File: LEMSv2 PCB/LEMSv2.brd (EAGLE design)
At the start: 160 x 100 mm, 83 parts, among them J2 M05, Q1 200mA/50V, Q10 200mA/50V, Q2 200mA/50V, Q3 200mA/50V, Q4 200mA/50V, Q5 200mA/50V, Q6 200mA/50V, Q7 200mA/50V, Q8 MMBT3904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

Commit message: Modified SD connector footprint, moved connectors
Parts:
- U1: value SDMMC06132 -> (none)
- moved J3 109.0 mm to (57.1, 17.1)
- moved J4 108.6 mm to (36.8, 17.1)
- moved J1 83.2 mm to (64.9, 42.5), turned to 270 degrees
- moved J5 78.9 mm to (54.6, 65.4)
- moved J6 73.4 mm to (30.2, 65.4)
- moved J2 61.7 mm to (40.6, 24.8)
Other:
- board outline removed

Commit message: Initial layout
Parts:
- removed D1: GREEN, LEMSv2:LED-0603
- removed D2: RED, LEMSv2:LED-0603
- added LED1: GREEN, LEMSv2:LED-0603
- added LED2: RED, LEMSv2:LED-0603
- C2, C3, C4, C5, C6, C7, C8, FB1: device LEMSv2:0805 -> LEMSv2:_0805
- J1: value (none) -> FEMALE 2x3; device LEMSv2:2X3_SMD -> LEMSv2:2X3
- J2: value M05 -> (none); device LEMSv2:1X05_SMD -> SparkFun-Connectors:1X05
- J3: device LEMSv2:1X06_SMD_STRAIGHT_COMBO -> LEMSv2:1X06
- J4, J5: device LEMSv2:1X08_SMD_COMBINED -> LEMSv2:1X08_ROUND
- J6: device LEMSv2:1X10_SMD_COMBINED -> LEMSv2:1X10
- moved U$3 173.9 mm to (81.3, 34.3), turned to 90 degrees
- moved U$1 156.4 mm to (81.3, 67.9)
- moved J26 152.6 mm to (80.6, 60.3), turned to 90 degrees
- moved C1 146.5 mm to (61.6, 35.6), turned to 270 degrees
- moved J17 139.8 mm to (73.8, 67.9), turned to 180 degrees
- moved Q9 138.4 mm to (64.8, 41.9)
- moved Q8 133.3 mm to (64.8, 46.4)
- moved R11 132.9 mm to (36.8, 24.1), turned to 180 degrees
- moved S1 132.4 mm to (81.3, 43.8), turned to 180 degrees
- moved J19 129.6 mm to (45.8, 67.9), turned to 180 degrees
- moved FID3 125.9 mm to (81.3, 71.8)
- moved Q3 124.4 mm to (76.2, 41.9), turned to 180 degrees
- moved R10 124.4 mm to (32.4, 24.1)
- moved J16 123.9 mm to (66.8, 67.9), turned to 180 degrees
- moved J27 122.5 mm to (49.6, 5.71)
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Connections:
- net N$10: now also LED2.A; no longer D2.A
- net N$7: now also LED1.C; no longer D1.C
- net N$8: now also LED2.C; no longer D2.C
- net N$9: now also LED1.A; no longer D1.A
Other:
- board outline added: 85.7 x 73.7 mm

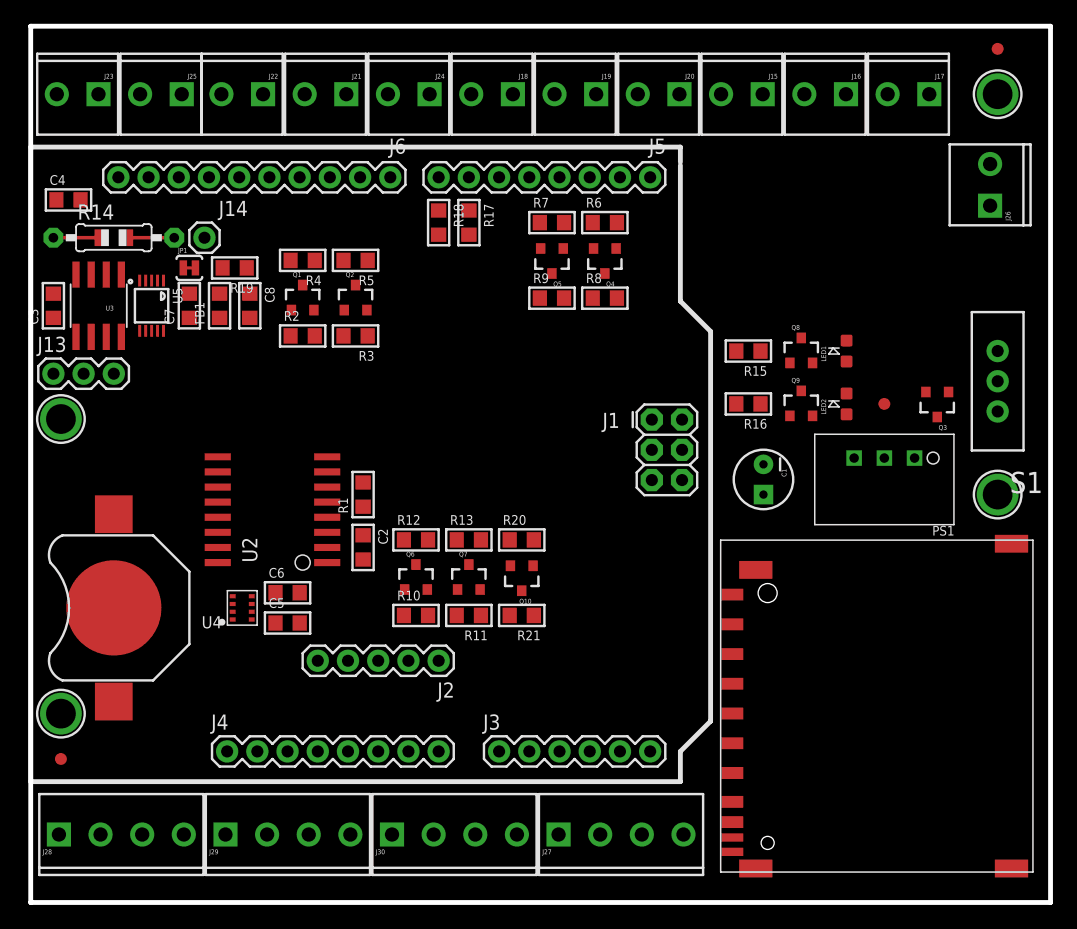
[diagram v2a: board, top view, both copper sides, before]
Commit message: 5TM library bug fix, board layout changes
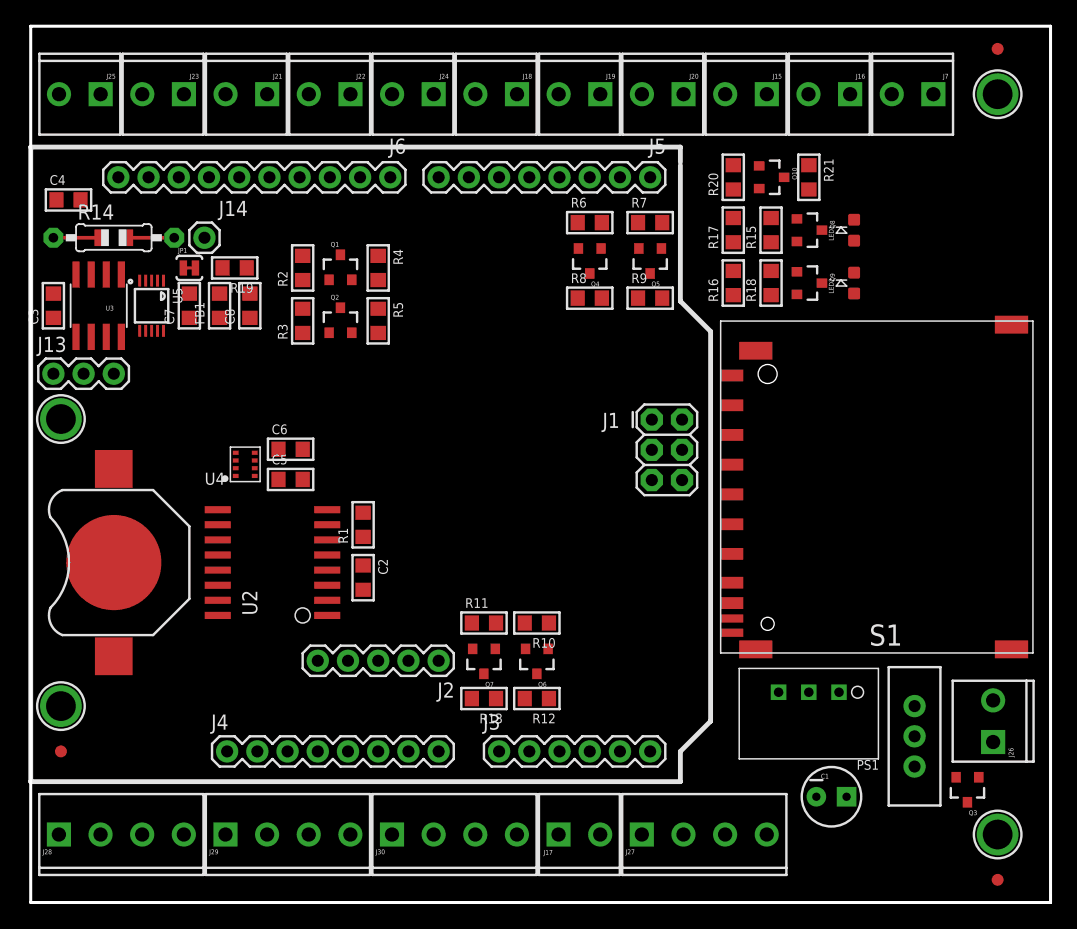
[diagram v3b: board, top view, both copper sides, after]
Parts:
- added J7: (no value), LEMSv2:SCREWTERMINAL-3.5MM-2
- moved J17 68.1 mm to (46.1, 5.71), turned to 0 degrees
- moved J26 45.1 mm to (80.9, 15.2)
- moved R21 44.0 mm to (65.4, 61.0), turned to 270 degrees
- moved FID1 41.1 mm to (81.3, 1.91)
- moved Q10 39.6 mm to (62.2, 61.0), turned to 270 degrees
- moved R20 35.3 mm to (59.1, 61.0), turned to 90 degrees
- moved Q3 32.5 mm to (78.7, 9.53)
- moved S1 30.7 mm to (74.3, 14.0), turned to 0 degrees
- moved U$3 28.6 mm to (81.3, 5.71)
- moved R18 28.4 mm to (62.2, 52.1), turned to 90 degrees
- moved C1 27.3 mm to (67.3, 8.89), turned to 0 degrees
- moved R17 22.2 mm to (59.1, 56.5), turned to 90 degrees
- moved PS1 20.7 mm to (65.4, 15.9)
- moved U1 18.4 mm to (71.1, 34.9)
- moved R12 16.8 mm to (42.5, 17.1), turned to 180 degrees
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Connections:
- new net FAN+: J7.1
- new net FAN-: J7.2
- net D10_5V: now also J16.1; no longer J27.4
- net GND: now also J27.1, U1.GP2, U1.GP4; no longer J16.1
- net MISO: now also J27.4; no longer J27.1
- net SCL_5V: now also J22.2; no longer J22.1
- net SDA_5V: now also J22.1; no longer J22.2

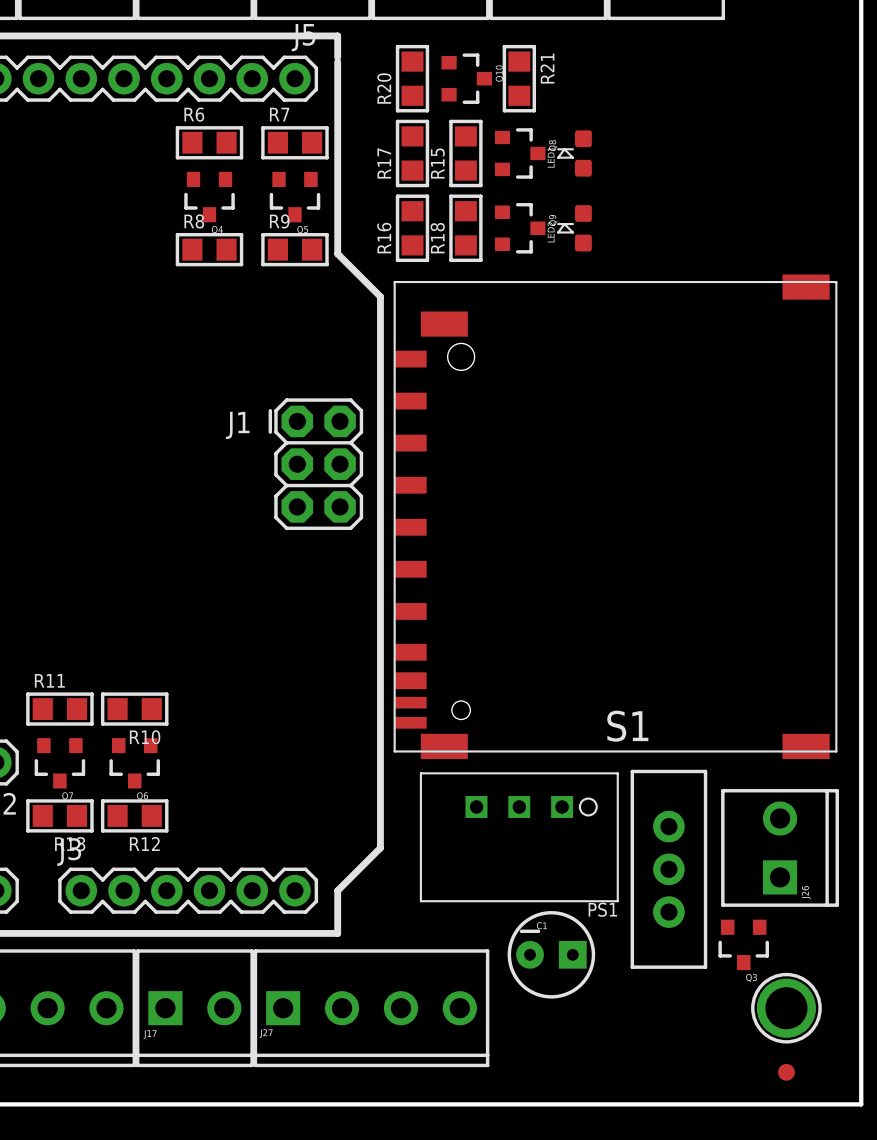
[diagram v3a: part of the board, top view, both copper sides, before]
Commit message: Switched 5TM power to transistor, added schottky
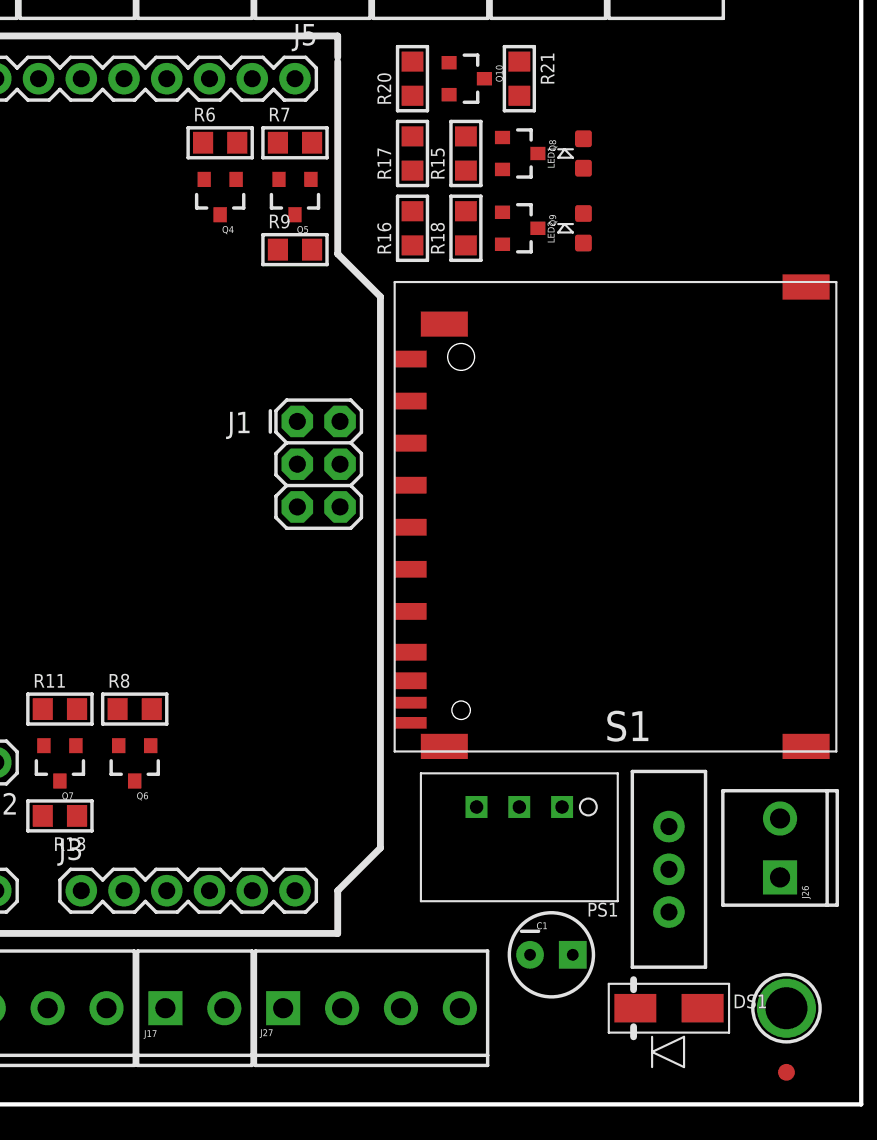
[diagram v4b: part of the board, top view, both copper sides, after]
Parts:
- removed Q3: 200mA/50V, LEMSv2:SOT23-3
- removed R10, R12: 10k, LEMSv2:_0805
- added DS1: DIODE_SCHOTTKY, LEMSv2:DO-214AC
- Q4, Q6: value 200mA/50V -> MMBT3904
- R6, R8: value 10k -> 1k
- moved R8 27.7 mm to (42.5, 23.5)
- moved Q4 0.63 mm to (47.6, 54.0)
- moved R6 0.63 mm to (47.6, 57.1)
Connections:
- removed net D2_5V: J15.1, Q4.3, R8.1
- removed net D38_5V: J17.1, Q6.3, R12.1
- removed net VBAT-: J26.2, Q3.3
- new net 5TM-: J27.1, Q6.3
- new net 5TM1-: J16.2, Q4.3
- new net N$11: Q4.1, R6.2
- new net N$12: Q6.1, R8.2
- new net N$13: DS1.C, S1.2
- net 3.3V: no longer Q4.1, Q6.1, R10.2, R6.2
- net 5V: now also J15.1, J17.1; no longer R12.2, R8.2
- net D2: no longer Q4.2
- net D38: now also R8.1; no longer Q6.2, R10.1
- net GND: now also J26.2, Q4.2, Q6.2; no longer J16.2, J27.1, Q3.2
- net VBAT+: now also DS1.A; no longer Q3.1, S1.2

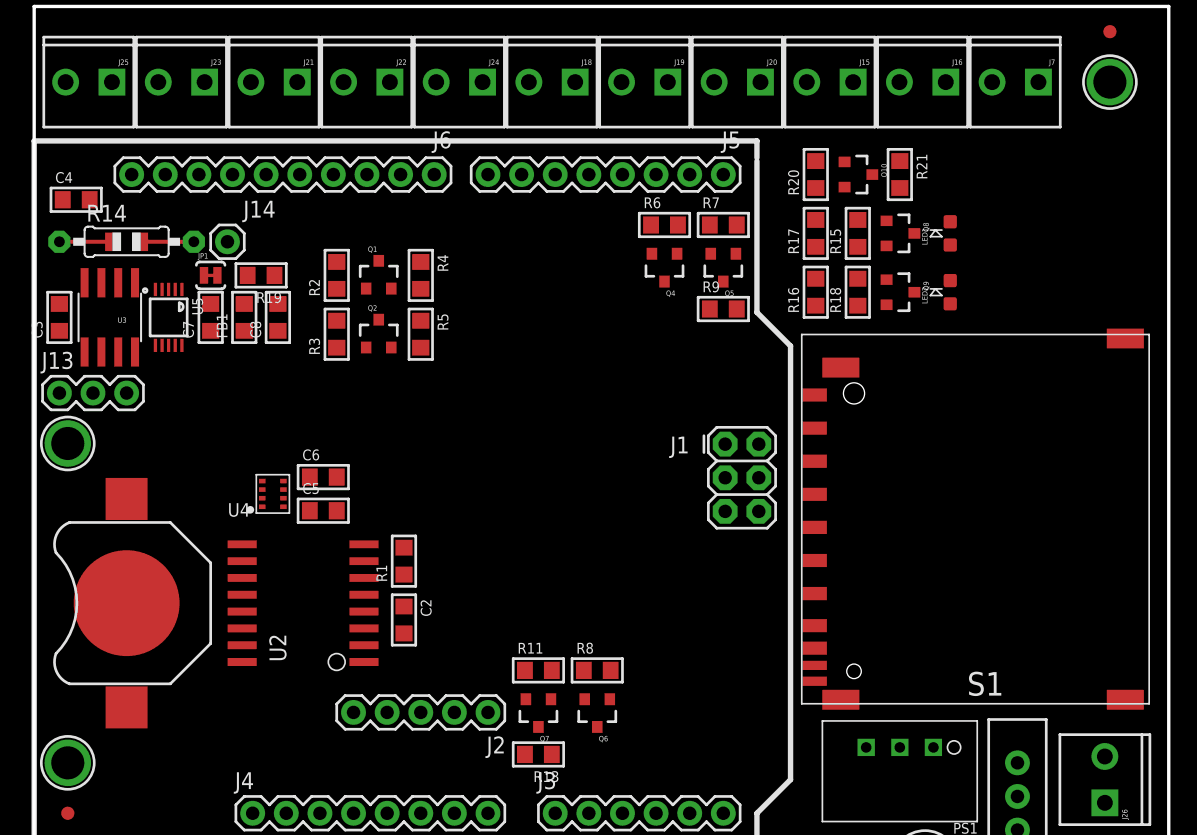
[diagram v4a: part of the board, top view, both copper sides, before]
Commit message: Started routing, part changes
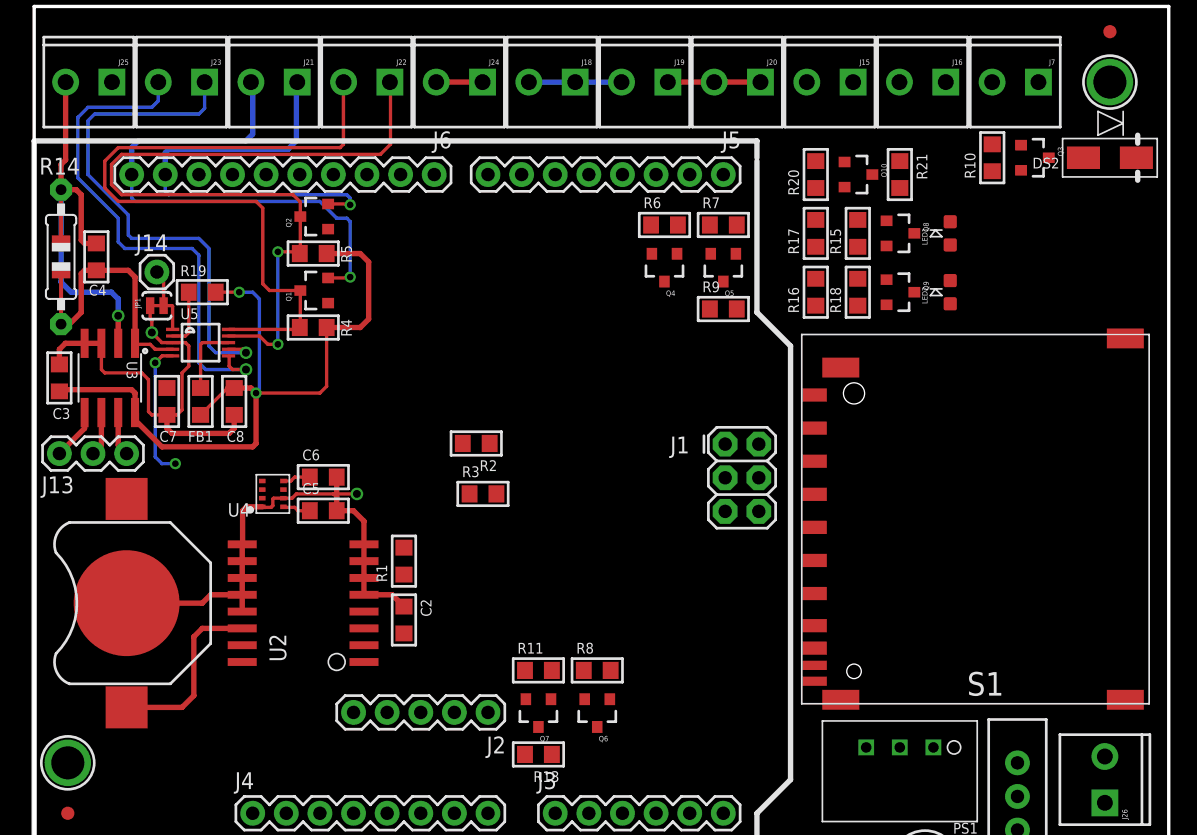
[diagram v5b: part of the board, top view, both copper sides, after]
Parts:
- removed U$4: MOUNTINGHOLE2.5, LEMSv2:MOUNTINGHOLE_2.5_PLATED
- added DS2: DIODE_SCHOTTKY, LEMSv2:DO-214AC
- added Q3: MMBT3904, LEMSv2:SOT23-3
- added R10: 4.3k, LEMSv2:_0805
- R17, R18, R6, R8: value 1k -> 4.3k
- moved R2 16.5 mm to (33.4, 40.6), turned to 180 degrees
- moved R3 16.4 mm to (33.9, 36.8), turned to 0 degrees
- moved R5 10.2 mm to (21.1, 55.0), turned to 0 degrees
- moved Q2 10.1 mm to (21.2, 57.8), turned to 90 degrees
- moved R4 9.03 mm to (21.1, 49.4), turned to 0 degrees
- moved C7 7.16 mm to (10.0, 43.8), turned to 270 degrees
- moved C8 7.16 mm to (15.1, 43.8), turned to 270 degrees
- moved FB1 7.16 mm to (12.6, 43.8), turned to 270 degrees
- moved J14 5.80 mm to (9.27, 53.6)
- moved R14 5.08 mm to (2.03, 54.7), turned to 270 degrees
- moved Q1 4.96 mm to (21.2, 52.2), turned to 90 degrees
- moved JP1 4.66 mm to (9.27, 51.1), turned to 180 degrees
- moved R19 4.62 mm to (12.7, 52.1)
- moved C4 4.58 mm to (4.70, 54.7), turned to 270 degrees
- moved J13 4.57 mm to (1.91, 39.9)
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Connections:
- net LIOUT renamed LI_OUT
- removed net FAN+: J7.1
- new net N$15: Q3.1, R10.2
- net 5V: now also DS2.C, J7.1
- net D11: now also R10.1
- net FAN-: now also DS2.A, Q3.3
- net GND: now also Q3.2
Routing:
- net GND: track 0.00 -> 80.4 mm, vias 0 -> 2
- net 5V: track 0.00 -> 62.4 mm, vias 0 -> 2
- net SDA_5V: track 0.00 -> 59.5 mm, vias 0 -> 2
- net SCL_5V: track 0.00 -> 54.9 mm
- net SCL: track 0.00 -> 40.9 mm, vias 0 -> 1
- net AIN3: track 0.00 -> 39.4 mm, vias 0 -> 1
- net AIN2: track 0.00 -> 39.3 mm, vias 0 -> 1
- net SDA: track 0.00 -> 34.0 mm, vias 0 -> 1
- net LI_IN-: track 0.00 -> 29.8 mm, vias 0 -> 1
- net 3.3V: track 0.00 -> 21.6 mm, vias 0 -> 2
- net LI_OUT: track 0.00 -> 17.2 mm
- net VBAT_RTC: track 0.00 -> 13.8 mm
- net N$14: track 0.00 -> 5.47 mm
- net ADDR: track 0.00 -> 5.20 mm
- net ALERT: track 0.00 -> 4.38 mm
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
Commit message: More routing
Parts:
- C2: value (none) -> 1uF
- C5, C6: value (none) -> 0.1uF
- moved R8 18.7 mm to (25.0, 16.9)
- moved Q6 13.8 mm to (29.2, 16.9), turned to 270 degrees
- moved R2 11.9 mm to (21.8, 43.3), turned to 270 degrees
- moved R3 10.7 mm to (25.4, 43.3), turned to 270 degrees
- moved R1 6.10 mm to (27.9, 25.7), turned to 270 degrees
- moved C2 3.30 mm to (27.9, 30.6), turned to 90 degrees
- moved R11 1.14 mm to (39.1, 23.0)
- moved Q7 1.09 mm to (39.1, 19.9)
- moved R13 1.02 mm to (39.1, 17.0)
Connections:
- new net RST2: J1.5
- net 5TM-: now also J17.2; no longer J27.1
- net D11: no longer R10.1
- net D4: now also R10.1
- net RST: no longer J1.5
- net SER_RX_5V: now also J27.1; no longer J17.2
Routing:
- net 5V: track 62.4 -> 232.9 mm, vias 2 -> 3
- net SDA: track 34.0 -> 138.0 mm, vias 1 -> 4
- net SCL: track 40.9 -> 123.5 mm, vias 1 -> 5
- net D8: track 0.00 -> 71.5 mm, vias 0 -> 1
- net A4: track 0.00 -> 52.9 mm
- net GND: track 80.4 -> 120.9 mm, vias 2 -> 3
- net D9: track 0.00 -> 39.7 mm, vias 0 -> 1
- net SER_RX_5V: track 0.00 -> 29.8 mm
- net 5TM-: track 0.00 -> 28.0 mm
- net N$1: track 0.00 -> 15.9 mm
- net SER_RX: track 0.00 -> 12.8 mm
- net VBAT+: track 0.00 -> 11.8 mm
- net N$13: track 0.00 -> 10.8 mm
- net 3.3V: track 21.6 -> 27.3 mm, vias 2 -> 4
- net D38: track 0.00 -> 3.48 mm
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- added copper zone on layer 1, net 3.3V
- added copper zone on layer 16, net GND

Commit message: More routing
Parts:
- added R12, R22: (no value), LEMSv2:_0805
- added R23, R24: 75k, LEMSv2:_0805
- moved R21 38.1 mm to (29.0, 49.8), turned to 180 degrees
- moved LED1 36.9 mm to (34.4, 44.3), turned to 0 degrees
- moved Q8 34.9 mm to (34.4, 40.5), turned to 0 degrees
- moved Q10 34.3 mm to (29.0, 52.8), turned to 180 degrees
- moved R15 33.8 mm to (34.4, 37.3), turned to 180 degrees
- moved R17 33.3 mm to (34.4, 34.2), turned to 180 degrees
- moved LED2 31.3 mm to (38.9, 44.3), turned to 0 degrees
- moved R20 30.5 mm to (29.0, 55.8), turned to 180 degrees
- moved Q9 28.9 mm to (38.9, 40.5), turned to 0 degrees
- moved R18 27.6 mm to (38.9, 37.3), turned to 180 degrees
- moved R16 27.0 mm to (38.9, 34.2), turned to 180 degrees
- moved Q4 21.8 mm to (67.8, 62.2), turned to 0 degrees
- moved R6 18.1 mm to (65.0, 62.2), turned to 90 degrees
- moved R9 15.2 mm to (62.1, 62.2), turned to 90 degrees
- moved Q5 10.8 mm to (59.1, 62.2), turned to 270 degrees
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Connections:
- new net N$17: R23.2, U1.8
- new net N$18: R24.2, U1.9
- net 3.3V: now also R23.1, R24.1
- net A5: now also R12.2, R22.1
- net GND: now also R22.2
- net VBAT+: now also R12.1
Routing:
- net 5V: track 232.9 -> 314.2 mm, vias 3 -> 4
- net D10_5V: track 0.00 -> 66.5 mm, vias 0 -> 1
- net MISO: track 0.00 -> 56.6 mm
- net SCK: track 0.00 -> 53.7 mm
- net MOSI: track 0.00 -> 40.9 mm
- net D5: track 0.00 -> 37.3 mm
- net D4: track 0.00 -> 34.7 mm
- net A5: track 0.00 -> 27.5 mm, vias 0 -> 1
- net GND: track 120.9 -> 142.4 mm, vias 3 -> 9
- net D2: track 0.00 -> 21.4 mm
- net D10: track 0.00 -> 12.3 mm
- net FAN-: track 0.00 -> 10.8 mm
- net VBAT+: track 11.8 -> 21.6 mm
- net SER1_RX_5V: track 0.00 -> 9.27 mm
- net 5TM1-: track 0.00 -> 6.44 mm
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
